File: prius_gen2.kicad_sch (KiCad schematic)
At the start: 31 parts, among them J1 Conn_02x05_Odd_Even, J2 Conn_01x06, Q1 IRLZ14SPBF, Q2 IRLZ14SPBF, SW1 SW_Push, SW2 SW_Push, U9 STM32F103VBTx, Y1 8MHz

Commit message: started adding AD2S
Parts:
- removed Q1, Q2: IRLZ14SPBF, Package_TO_SOT_SMD:TO-252-2, symbol prius_gen2-rescue:IRLZ34N-Transistor_FET-prius_gen2-rescue
- removed R62, R63: 10k, Resistor_SMD:R_0603_1608Metric, symbol prius_gen2-rescue:R-Device-prius_gen2-rescue
- removed U9: STM32F103VBTx, Package_QFP:LQFP-100_14x14mm_P0.5mm, symbol prius_gen2-rescue:STM32F103VBTx-MCU_ST_STM32F1-prius_gen2-rescue
- added TP1, TP2, TP3, TP4, TP5, TP6, TP7: TestPoint, TestPoint:TestPoint_Keystone_5000-5004_Miniature, symbol Connector:TestPoint
- added U1: STM32F407VETx, Package_QFP:LQFP-100_14x14mm_P0.5mm, symbol MCU_ST_STM32F4:STM32F407VETx
- C1, C2: symbol prius_gen2-rescue:C-Device-prius_gen2-rescue -> Device:C
- C6: renamed from C12; symbol prius_gen2-rescue:C-Device-prius_gen2-rescue -> Device:C
- R1, R4: symbol prius_gen2-rescue:R-Device-prius_gen2-rescue -> Device:R
- R2: renamed from R3; symbol prius_gen2-rescue:R-Device-prius_gen2-rescue -> Device:R
- R3: renamed from R5; symbol prius_gen2-rescue:R-Device-prius_gen2-rescue -> Device:R
- R5: renamed from R64; symbol prius_gen2-rescue:R-Device-prius_gen2-rescue -> Device:R
- R6: renamed from R2; symbol prius_gen2-rescue:R-Device-prius_gen2-rescue -> Device:R
- Y1: symbol prius_gen2-rescue:Crystal-Device-prius_gen2-rescue -> Device:Crystal
- renumbered C7 to C10, C8 to C11, C9 to C12, C10 to C3, C11 to C5, C3 to C7, C5 to C8, C6 to C9, D7 to D1, D1 to D2
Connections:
- net +3V3: now also U1.100 (VDD), U1.11 (VDD), U1.19 (VDD), U1.28 (VDD), U1.50 (VDD), U1.75 (VDD)
- net ADC12: now also U1.17 (PC2)
- net ADC13: now also U1.18 (PC3)
- net ADC14: now also U1.33 (PC4)
- net ADC5: now also U1.30 (PA5)
- net ADC8: now also U1.35 (PB0)
- net ADC9: now also U1.36 (PB1)
- net CAN_RX: now also U1.70 (PA11)
- net CAN_TX: now also U1.71 (PA12)
- net GND: now also U1.10 (VSS), U1.20 (VSSA), U1.27 (VSS), U1.74 (VSS), U1.99 (VSS)
- net PC13: now also U1.7 (PC13)
- net SWCLK: now also U1.76 (PA14)
- net SWDIO: now also U1.72 (PA13)
- net TIM1_BKIN: now also TP7.1, U1.51 (PB12), U1.66 (PC9)
- net TIM1_CH1: now also TP6.1, U1.67 (PA8)
- net TIM1_CH2: now also TP5.1, U1.68 (PA9)
- net TIM1_CH2N: now also TP2.1, U1.53 (PB14)
- net TIM1_CH3: now also TP4.1, U1.69 (PA10)
- net TIM2_CH2: now also U1.24 (PA1)
- net TIM3_CH1: now also U1.31 (PA6)
- net TIM3_CH2: now also U1.32 (PA7)
- net TIM3_ETR: now also U1.83 (PD2)
- net UART3_RX: now also U1.48 (PB11)
- net UART3_TX: now also U1.47 (PB10)
- net VDDA: now also U1.21 (VREF+), U1.22 (VDDA)
- net nRESET: now also U1.14 (NRST)
- net at D2.1 (K): now also U1.80 (PC12)
- net at C1.2, Y1.1: now also U1.12 (PH0)
- net at C2.2, Y1.2: now also U1.13 (PH1)
- net at D1.1 (K): now also U1.78 (PC10)
- net at R2.1, SW1.2: now also U1.94 (BOOT0)
- new net MISO: U1.90 (PB4)
- new net SCLK: U1.89 (PB3)
- new net TIM1_CH1N: TP1.1, U1.52 (PB13)
- new net TIM1_CH3N: TP3.1, U1.54 (PB15)
- new net ~{CS}: U1.91 (PB5)
- new net ~{SAMPLE}: U1.92 (PB6)
- no-connect marks 52 -> 4
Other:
- sheet Connectors ports: added none; removed OUT_DCSW, OUT_PRE, SIG_BRAKE, SIG_FWD, SIG_REV, SIG_START, THROTTLE1, THROTTLE2, TIM1_CH2N
- sheet Input Filter ports: added none; removed ADC10, ADC11, ADC2, ADC3, ADC4, REV, SIG_BRAKE, SIG_FWD, SIG_REV, SIG_START, THROTTLE1, THROTTLE2, TIM4_CH1
- sheet Resolver ports: added COS, SCLK, SIN, SO, ~{COS}, ~{RD}, ~{SAMPLE}, ~{SIN}; removed R1, R2, TIM3_ETR
- moved on the sheet: C1, C10, C11, C12, C2, C3, C4, C5, C6, C7, C8, C9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

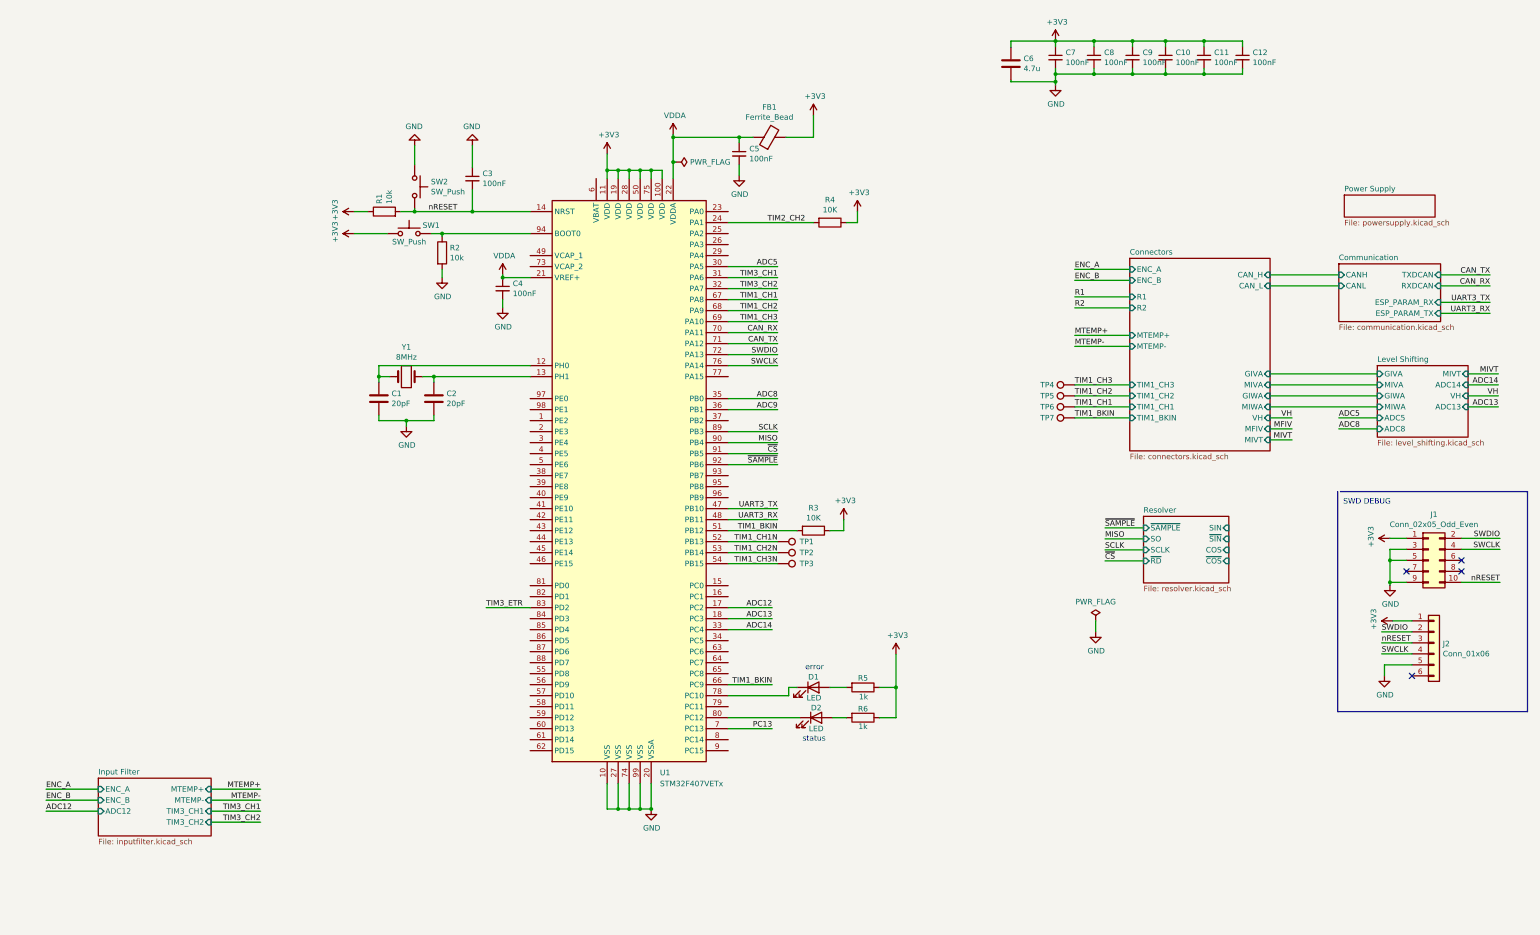
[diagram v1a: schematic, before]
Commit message: routed ad2s
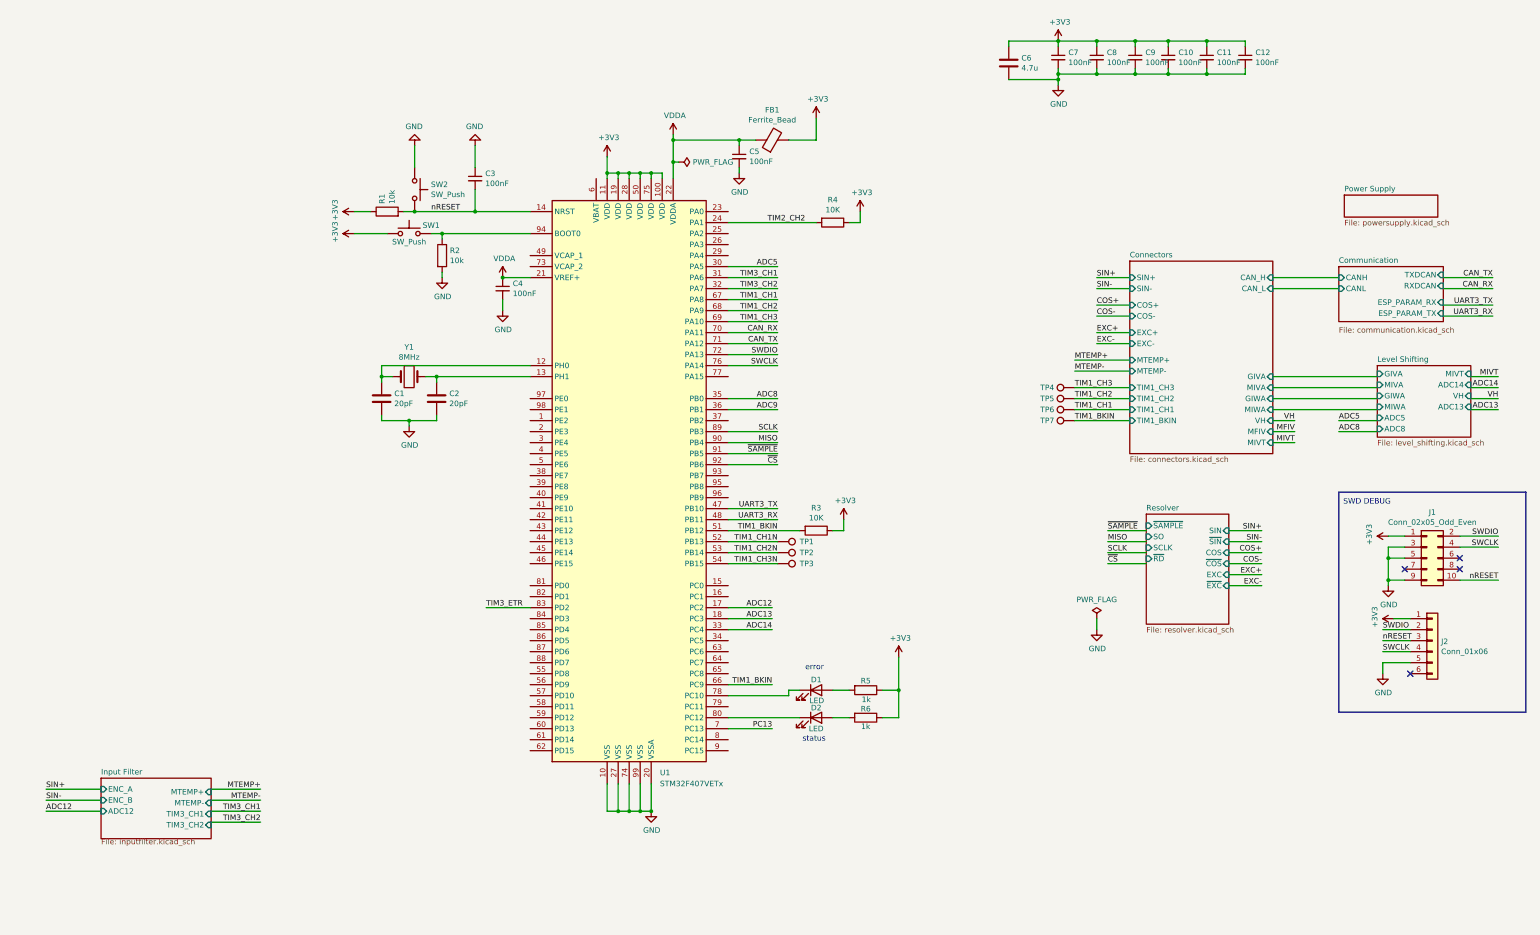
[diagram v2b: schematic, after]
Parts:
- R1, R2, R3, R4: LCSC (none) -> C25804
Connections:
- net ~{CS}: now also U1.92 (PB6); no longer U1.91 (PB5)
- net ~{SAMPLE}: now also U1.91 (PB5); no longer U1.92 (PB6)
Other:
- sheet Connectors ports: added COS+, COS-, EXC+, EXC-, SIN+, SIN-; removed ENC_A, ENC_B, R1, R2
- sheet Resolver ports: added EXC, ~{EXC}; removed none
- moved on the sheet: C1, C10, C11, C12, C2, C3, C5, C6, C7, C8, C9, D1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

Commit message: cleaned up board
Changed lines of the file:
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@@
     (stroke (width 0) (type default) (color 0 0 0 0))
   )
-  (wire (pts (xy 373.38 124.46) (xy 361.95 124.46))
+  (wire (pts (xy 373.38 123.825) (xy 361.95 123.825))
     (stroke (width 0) (type default) (color 0 0 0 0))
   )
@@
     (stroke (width 0) (type default) (color 0 0 0 0))
   )
-  (wire (pts (xy 361.95 121.92) (xy 373.38 121.92))
+  (wire (pts (xy 361.95 121.285) (xy 373.38 121.285))
     (stroke (width 0) (type default) (color 0 0 0 0))
   )
@@
     (stroke (width 0) (type default) (color 0 0 0 0))
   )
-  (wire (pts (xy 284.48 176.53) (xy 293.37 176.53))
-    (stroke (width 0) (type default) (color 0 0 0 0))
-  )
-  (wire (pts (xy 88.9 233.68) (xy 77.47 233.68))
+  (wire (pts (xy 284.48 175.26) (xy 293.37 175.26))
+    (stroke (width 0) (type default) (color 0 0 0 0))
+  )
+  (wire (pts (xy 88.9 234.315) (xy 77.47 234.315))
     (stroke (width 0) (type default) (color 0 0 0 0))
   )
@@
     (stroke (width 0) (type default) (color 0 0 0 0))
   )
-  (wire (pts (xy 88.9 236.22) (xy 77.47 236.22))
+  (wire (pts (xy 88.9 236.855) (xy 77.47 236.855))
     (stroke (width 0) (type default) (color 0 0 0 0))
   )
@@
     (stroke (width 0) (type default) (color 0 0 0 0))
   )
-  (wire (pts (xy 361.95 115.57) (xy 373.38 115.57))
+  (wire (pts (xy 361.95 114.935) (xy 373.38 114.935))
     (stroke (width 0) (type default) (color 0 0 0 0))
   )
@@
     (stroke (width 0) (type default) (color 0 0 0 0))
   )
-  (wire (pts (xy 88.9 241.3) (xy 77.47 241.3))
+  (wire (pts (xy 88.9 241.935) (xy 77.47 241.935))
     (stroke (width 0) (type default) (color 0 0 0 0))
   )
@@
     (stroke (width 0) (type default) (color 0 0 0 0))
   )
-  (wire (pts (xy 284.48 181.61) (xy 293.37 181.61))
+  (wire (pts (xy 284.48 180.34) (xy 293.37 180.34))
     (stroke (width 0) (type default) (color 0 0 0 0))
   )
@@
     (stroke (width 0) (type default) (color 0 0 0 0))
   )
-  (wire (pts (xy 284.48 173.99) (xy 293.37 173.99))
+  (wire (pts (xy 284.48 172.72) (xy 293.37 172.72))
     (stroke (width 0) (type default) (color 0 0 0 0))
   )
@@
     (stroke (width 0) (type default) (color 0 0 0 0))
   )
-  (wire (pts (xy 284.48 179.07) (xy 293.37 179.07))
+  (wire (pts (xy 284.48 177.8) (xy 293.37 177.8))
     (stroke (width 0) (type default) (color 0 0 0 0))
   )
@@
     (stroke (width 0) (type default) (color 0 0 0 0))
   )
-  (wire (pts (xy 373.38 118.11) (xy 361.95 118.11))
+  (wire (pts (xy 373.38 117.475) (xy 361.95 117.475))
     (stroke (width 0) (type default) (color 0 0 0 0))
   )
@@
     (stroke (width 0) (type default) (color 0 0 0 0))
   )
-  (wire (pts (xy 88.9 238.76) (xy 77.47 238.76))
+  (wire (pts (xy 88.9 239.395) (xy 77.47 239.395))
     (stroke (width 0) (type default) (color 0 0 0 0))
   )
@@
     (effects (font (size 1.27 1.27)) (justify left bottom))
   )
-  (label "UART3_RX" (at 373.38 124.46 180)
+  (label "UART3_RX" (at 373.38 123.825 180)
     (effects (font (size 1.27 1.27)) (justify right bottom))
   )
@@
     (effects (font (size 1.27 1.27)) (justify left bottom))
   )
-  (label "TIM3_CH2" (at 88.9 241.3 180)
+  (label "TIM3_CH2" (at 88.9 241.935 180)
     (effects (font (size 1.27 1.27)) (justify right bottom))
   )
@@
     (effects (font (size 1.27 1.27)) (justify right bottom))
   )
-  (label "SCLK" (at 284.48 179.07 0)
-    (effects (font (size 1.27 1.27)) (justify left bottom))
-  )
-  (label "~{CS}" (at 284.48 181.61 0)
+  (label "SCLK" (at 284.48 177.8 0)
+    (effects (font (size 1.27 1.27)) (justify left bottom))
+  )
+  (label "~{CS}" (at 284.48 180.34 0)
     (effects (font (size 1.27 1.27)) (justify left bottom))
   )
@@
     (effects (font (size 1.27 1.27)) (justify right bottom))
   )
-  (label "MTEMP+" (at 88.9 233.68 180)
-    (effects (font (size 1.27 1.27)) (justify right bottom))
-  )
-  (label "~{SAMPLE}" (at 284.48 173.99 0)
+  (label "MTEMP+" (at 88.9 234.315 180)
+    (effects (font (size 1.27 1.27)) (justify right bottom))
+  )
+  (label "~{SAMPLE}" (at 284.48 172.72 0)
     (effects (font (size 1.27 1.27)) (justify left bottom))
   )
@@
     (effects (font (size 1.27 1.27)) (justify right bottom))
   )
-  (label "CAN_TX" (at 373.38 115.57 180)
+  (label "CAN_TX" (at 373.38 114.935 180)
     (effects (font (size 1.27 1.27)) (justify right bottom))
   )
@@
     (effects (font (size 1.27 1.27)) (justify right bottom))
   )
-  (label "UART3_TX" (at 373.38 121.92 180)
+  (label "UART3_TX" (at 373.38 121.285 180)
     (effects (font (size 1.27 1.27)) (justify right bottom))
   )
@@
     (effects (font (size 1.27 1.27)) (justify right bottom))
   )
-  (label "TIM3_CH1" (at 88.9 238.76 180)
+  (label "TIM3_CH1" (at 88.9 239.395 180)
     (effects (font (size 1.27 1.27)) (justify right bottom))
   )
@@
     (effects (font (size 1.27 1.27)) (justify left bottom))
   )
-  (label "MTEMP-" (at 88.9 236.22 180)
+  (label "MTEMP-" (at 88.9 236.855 180)
     (effects (font (size 1.27 1.27)) (justify right bottom))
   )
@@
     (effects (font (size 1.27 1.27)) (justify right bottom))
   )
-  (label "CAN_RX" (at 373.38 118.11 180)
+  (label "CAN_RX" (at 373.38 117.475 180)
     (effects (font (size 1.27 1.27)) (justify right bottom))
   )
@@
     (effects (font (size 1.27 1.27)) (justify right bottom))
   )
-  (label "MISO" (at 284.48 176.53 0)
+  (label "MISO" (at 284.48 175.26 0)
     (effects (font (size 1.27 1.27)) (justify left bottom))
   )
@@
       (effects (font (size 1.27 1.27)) (justify left top))
     )
-    (pin "~{SAMPLE}" input (at 293.37 172.847 180)
-      (effects (font (size 1.27 1.27)) (justify left))
-    )
-    (pin "~{RD}" input (at 293.37 180.467 180)
+    (pin "~{SAMPLE}" input (at 293.37 172.72 180)
+      (effects (font (size 1.27 1.27)) (justify left))
+    )
+    (pin "~{RD}" input (at 293.37 180.34 180)
       (effects (font (size 1.27 1.27)) (justify left))
     )
@@
       (effects (font (size 1.27 1.27)) (justify right))
     )
-    (pin "SO" input (at 293.37 175.387 180)
-      (effects (font (size 1.27 1.27)) (justify left))
-    )
-    (pin "SCLK" input (at 293.37 177.927 180)
+    (pin "SO" input (at 293.37 175.26 180)
+      (effects (font (size 1.27 1.27)) (justify left))
+    )
+    (pin "SCLK" input (at 293.37 177.8 180)
       (effects (font (size 1.27 1.27)) (justify left))
     )
@@
     )
   )
-  (sheet (at 346.71 135.89) (size 21.59 16.51) (fields_autoplaced)
+  (sheet (at 346.71 136.525) (size 21.59 16.51) (fields_autoplaced)
     (stroke (width 0) (type solid) (color 0 0 0 0))
     (fill (color 0 0 0 0.0000))
-    (property "Sheet name" "Level Shifting" (id 0) (at 346.71 135.1784 0)
+    (property "Sheet name" "Level Shifting" (id 0) (at 346.71 135.8134 0)
       (effects (font (size 1.27 1.27)) (justify left bottom))
     )
-    (property "Sheet file" "level_shifting.kicad_sch" (id 1) (at 346.71 152.9846 0)
+    (property "Sheet file" "level_shifting.kicad_sch" (id 1) (at 346.71 153.6196 0)
       (effects (font (size 1.27 1.27)) (justify left top))
     )
-    (pin "GIVA" input (at 346.71 137.795 180)
-      (effects (font (size 1.27 1.27)) (justify left))
-    )
-    (pin "MIVA" input (at 346.71 140.335 180)
-      (effects (font (size 1.27 1.27)) (justify left))
-    )
-    (pin "GIWA" input (at 346.71 142.875 180)
-      (effects (font (size 1.27 1.27)) (justify left))
-    )
-    (pin "MIWA" input (at 346.71 145.415 180)
-      (effects (font (size 1.27 1.27)) (justify left))
-    )
-    (pin "ADC5" input (at 346.71 147.955 180)
-      (effects (font (size 1.27 1.27)) (justify left))
-    )
-    (pin "ADC8" input (at 346.71 150.495 180)
-      (effects (font (size 1.27 1.27)) (justify left))
-    )
-    (pin "MIVT" input (at 368.3 137.795 0)
-      (effects (font (size 1.27 1.27)) (justify right))
-    )
-    (pin "ADC14" input (at 368.3 140.335 0)
-      (effects (font (size 1.27 1.27)) (justify right))
-    )
-    (pin "VH" input (at 368.3 142.875 0)
-      (effects (font (size 1.27 1.27)) (justify right))
-    )
-    (pin "ADC13" input (at 368.3 145.415 0)
-      (effects (font (size 1.27 1.27)) (justify right))
-    )
+    (pin "GIVA" input (at 346.71 138.43 180)
+      (effects (font (size 1.27 1.27)) (justify left))
+    )
+    (pin "MIVA" input (at 346.71 140.97 180)
+      (effects (font (size 1.27 1.27)) (justify left))
+    )
+    (pin "GIWA" input (at 346.71 143.51 180)
+      (effects (font (size 1.27 1.27)) (justify left))
+    )
+    (pin "MIWA" input (at 346.71 146.05 180)
+      (effects (font (size 1.27 1.27)) (justify left))
+    )
+    (pin "ADC5" input (at 346.71 148.59 180)
+      (effects (font (size 1.27 1.27)) (justify left))
+    )
+    (pin "ADC8" input (at 346.71 151.13 180)
+      (effects (font (size 1.27 1.27)) (justify left))
+    )
+    (pin "MIVT" input (at 368.3 138.43 0)
+      (effects (font (size 1.27 1.27)) (justify right))
+    )
+    (pin "ADC14" input (at 368.3 140.97 0)
+      (effects (font (size 1.27 1.27)) (justify right))
+    )
+    (pin "VH" input (at 368.3 143.51 0)
+      (effects (font (size 1.27 1.27)) (justify right))
+    )
+    (pin "ADC13" input (at 368.3 146.05 0)
+      (effects (font (size 1.27 1.27)) (justify right))
+    )

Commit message: added USB
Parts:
- added C16: 100n, Capacitor_SMD:C_0603_1608Metric, symbol Device:C
- added D11: schottky, Diode_SMD:D_SOD-123, symbol Device:D_Schottky_Small
- added J5: ~, Connector_PinSocket_2.54mm:PinSocket_1x05_P2.54mm_Vertical, symbol Connector_Generic:Conn_01x05
- added R14: 100k, Resistor_SMD:R_0402_1005Metric, symbol Device:R
- added U9: ~, Package_TO_SOT_SMD:SOT-23-6, symbol Power_Protection:USBLC6-2SC6
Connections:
- net CAN_RX: now also U1.95 (PB8); no longer U1.70 (PA11)
- net CAN_TX: now also U1.96 (PB9); no longer U1.71 (PA12)
- net GND: now also C16.2, J5.4 (Pin_4), R14.2, U9.2 (GND)
- new net: D11.2 (A), J5.1 (Pin_1), U9.5 (VBUS)
- new net +5V: D11.1 (K)
- new net USB_D+: J5.3 (Pin_3), U1.71 (PA12), U9.1 (I/O1), U9.6 (I/O1)
- new net USB_D-: J5.2 (Pin_2), U1.70 (PA11), U9.3 (I/O2), U9.4 (I/O2)
- new net USB_SHIELD: C16.1, J5.5 (Pin_5), R14.1
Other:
- note added: "Pin header"
- note added: "USB"

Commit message: fixes for v5
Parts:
- removed J1: Conn_02x05_Odd_Even, Connector_PinHeader_1.27mm:PinHeader_2x05_P1.27mm_Vertical_SMD, symbol prius_gen2-rescue:Conn_02x05_Odd_Even-Connector_Generic-prius_gen2-rescue
- added C26, C27: 2.2uF, Capacitor_SMD:C_0603_1608Metric, symbol Device:C
- added TP8, TP9: TestPoint, TestPoint:TestPoint_Keystone_5000-5004_Miniature, symbol Connector:TestPoint
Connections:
- net +3V3: now also U1.6 (VBAT)
- net GND: now also C26.2, C27.2
- net UART3_RX: now also TP9.1
- net UART3_TX: now also TP8.1
- net at U1.49 (VCAP_1): now also C27.1
- net at U1.73 (VCAP_2): now also C26.1
- no-connect marks 4 -> 48
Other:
- sheet Communication ports: added none; removed ESP_PARAM_RX, ESP_PARAM_TX
- moved on the sheet: J2, R2, R3, SW1

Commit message: more updates for v0.5 prod
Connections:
- net MISO: now also U1.79 (PC11); no longer U1.90 (PB4)
- net SCLK: now also U1.78 (PC10); no longer U1.89 (PB3)
- net at D2.1 (K): now also U1.77 (PA15); no longer U1.80 (PC12)
- net at D1.1 (K): now also U1.65 (PC8); no longer U1.78 (PC10)
- no-connect marks 48 -> 47
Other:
- moved on the sheet: D1, D2, R5, R6
